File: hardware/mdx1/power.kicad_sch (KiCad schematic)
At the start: 110 parts, among them J1 USB-C 16P, J2 USBLC6-2SC6 (USB ESD), J3 Battery JST-PH 3p, Q1 SiR626DP (60V), Q2 BSC190N15NS3 (150V), Q3 BSS127S (600V), U1 BQ24075RGT, U2 BQ27441-G1A, U3 TPS63001 (3.3V), U4 TPS65131RGE, U5 LT3045 (+5VA), U6 LT3094 (-5VA), U7 TPS7A2033 (+3V3A), U8 LT3757 (VTX 8-30V), U9 LT3757 (VBRIDGE 100V)

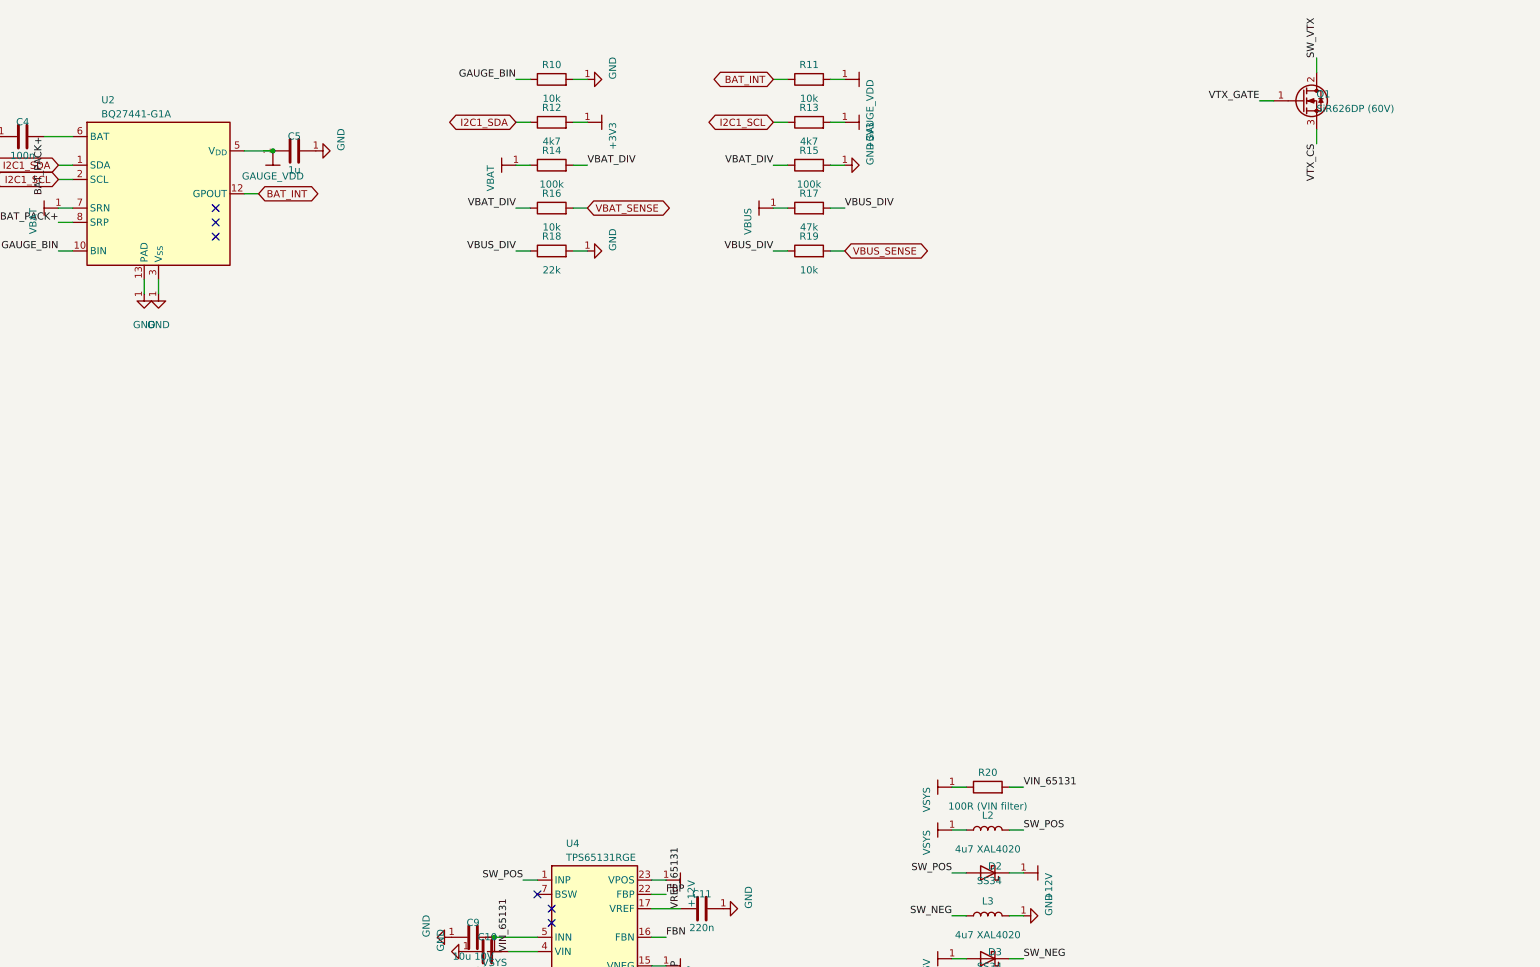
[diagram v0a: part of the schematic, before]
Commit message: Re-source out-of-stock parts; rework D8/9 footprint and GNSS antenna front end
Parts re-sourced to in-stock equivalents (BOM + board + firmware kept in sync):
- U4  TPS65131RGET, U12 INA241A2QDGKRQ1, U23 LSM6DSO32TR (same footprints)
- Q1  SiR680ADP-T1-UE3 (80 V, same PowerPAK SO-8; higher Qg - verify gate drive)
- U2  BQ27441DRZT-G1A (drop-in, R9 sense retained)
- D8/9 NSVBAT54SWT1G: SOT-323/SC-70 dual-series wired as a single diode
  (anode=pin1, cathode=pin3, pin2 NC); footprint changed on the board
- C32/C33/C38-48 re-sourced (KEMET/Murata/TDK), same footprints

GNSS antenna: chip antenna -> external active antenna via u.FL
- Removed U28 (chip antenna), C115 (match pad), R111 (0R RF series-match)
- Added J13 u.FL (Molex 73412-0110) + bias-tee: L8 27nH feed, C127 33pF DC block,
  C128 10nF VCC_RF bypass, D17 PESD0402-140 ESD (verify Vrwm >= 5 V)

Firmware:
- mdx_config.h: MDX_ITX_V_PER_A 0.4 -> 1.0 (INA241A2 is 50 V/V, not 20)
- hal_stm32.c: LSM6DSO32 accel init 0x48 -> 0x40 (FS_XL encoding differs; keeps +-4 g)
- make test: 96 checks pass

BOM: bom_data.json reconciled to the updated board (every placed part has an MPN;
fab BOM drops only the 15 test points). Regenerated JLCPCB fab package and the
DigiKey upload BOM (grouped by MPN, compact references).
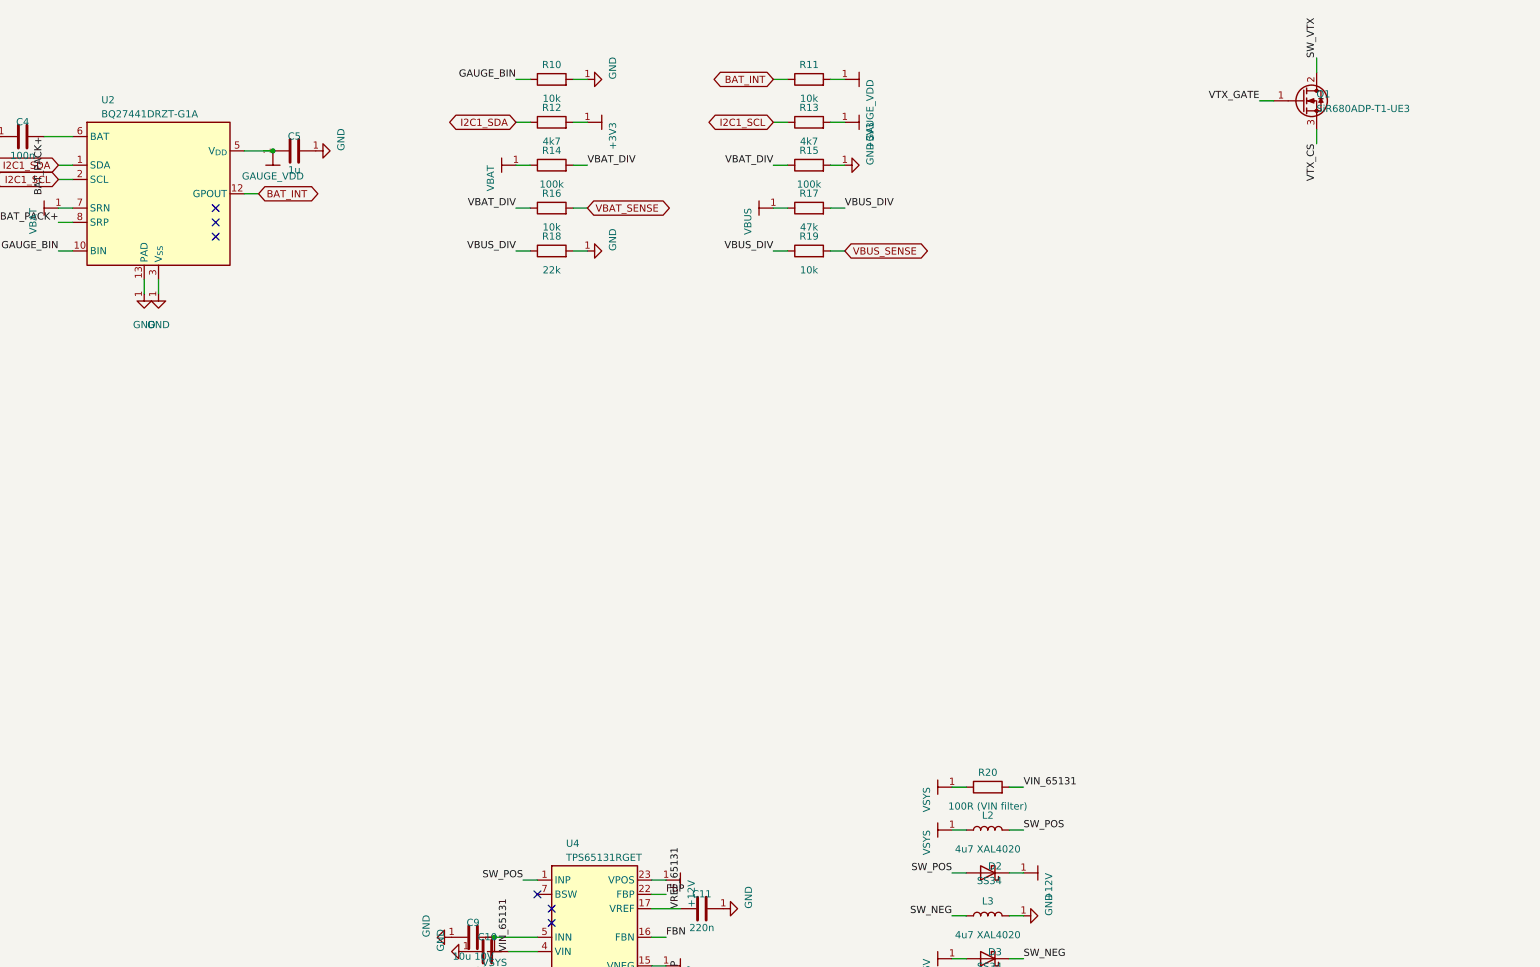
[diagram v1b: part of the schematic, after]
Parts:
- Q1: value SiR626DP (60V) -> SiR680ADP-T1-UE3
- U2: value BQ27441-G1A -> BQ27441DRZT-G1A
- U4: value TPS65131RGE -> TPS65131RGET
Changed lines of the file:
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@@
 			)
 		)
-		(property "Value" "BQ27441-G1A"
+		(property "Value" "BQ27441DRZT-G1A"
 			(at -453.39 242.38 0)
 			(show_name no)
@@
 			)
 		)
-		(property "Value" "TPS65131RGE"
+		(property "Value" "TPS65131RGET"
 			(at -370.84 374.46 0)
 			(show_name no)
@@
 			)
 		)
-		(property "Value" "SiR626DP (60V)"
+		(property "Value" "SiR680ADP-T1-UE3"
 			(at -237.53 241.43 0)
 			(show_name no)
